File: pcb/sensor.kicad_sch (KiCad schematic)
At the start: 3 parts, among them U1 HAL9303SO

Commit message: pcb: specify component's LCSC part number
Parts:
- C1: LCSC Part # (none) -> C1591
- R1: LCSC Part # (none) -> C22775
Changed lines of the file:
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@@
+			)
+		)
+		(property "LCSC Part #" "C22775"
+			(at 104.14 54.61 0)
+			(effects
+				(font
+					(size 1.27 1.27)
+				)
+				(hide yes)
 			)
 		)
@@
 			(at 88.9 54.61 0)
 			(effects
+				(font
+					(size 1.27 1.27)
+				)
+				(hide yes)
+			)
+		)
+		(property "LCSC Part #" "C1591"
+			(at 88.9 54.61 0)
+			(effects

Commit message: pcb: match component footprint with their actual size
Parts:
- C1: LCSC Part # C1591 -> C160831
- R1: LCSC Part # C22775 -> C304499
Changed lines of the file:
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@@
 			)
 		)
-		(property "LCSC Part #" "C22775"
+		(property "LCSC Part #" "C304499"
 			(at 104.14 54.61 0)
 			(effects
@@
 			)
 		)
-		(property "LCSC Part #" "C1591"
+		(property "LCSC Part #" "C160831"
 			(at 88.9 54.61 0)
 			(effects

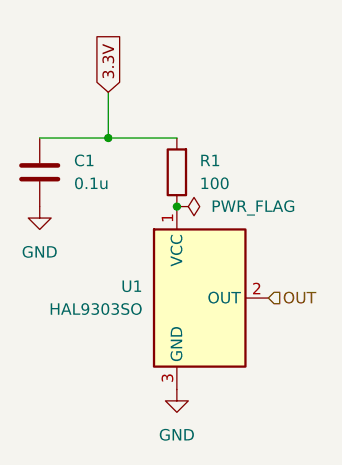
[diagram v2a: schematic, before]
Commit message: pcb: use cheaper hall effect sensor and remove unnecessary capacitor and resistor connected to each sensor
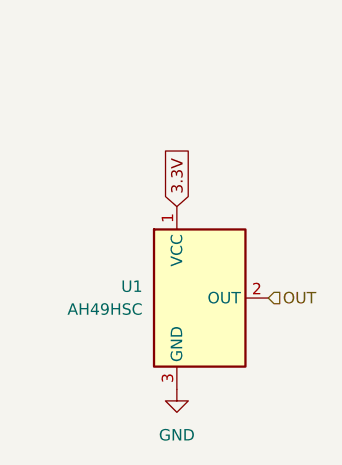
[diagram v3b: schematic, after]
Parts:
- removed C1: 0.1u, Capacitor_SMD:C_0201_0603Metric, symbol Device:C
- removed R1: 100, Resistor_SMD:R_0201_0603Metric, symbol Device:R
- U1: value HAL9303SO -> AH49HSC; LCSC Part # (none) -> C510723
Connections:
- net 3.3V: now also U1.1 (VCC)
